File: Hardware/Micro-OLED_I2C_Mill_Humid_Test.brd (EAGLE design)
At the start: 20.3 x 29.2 mm, 5 parts

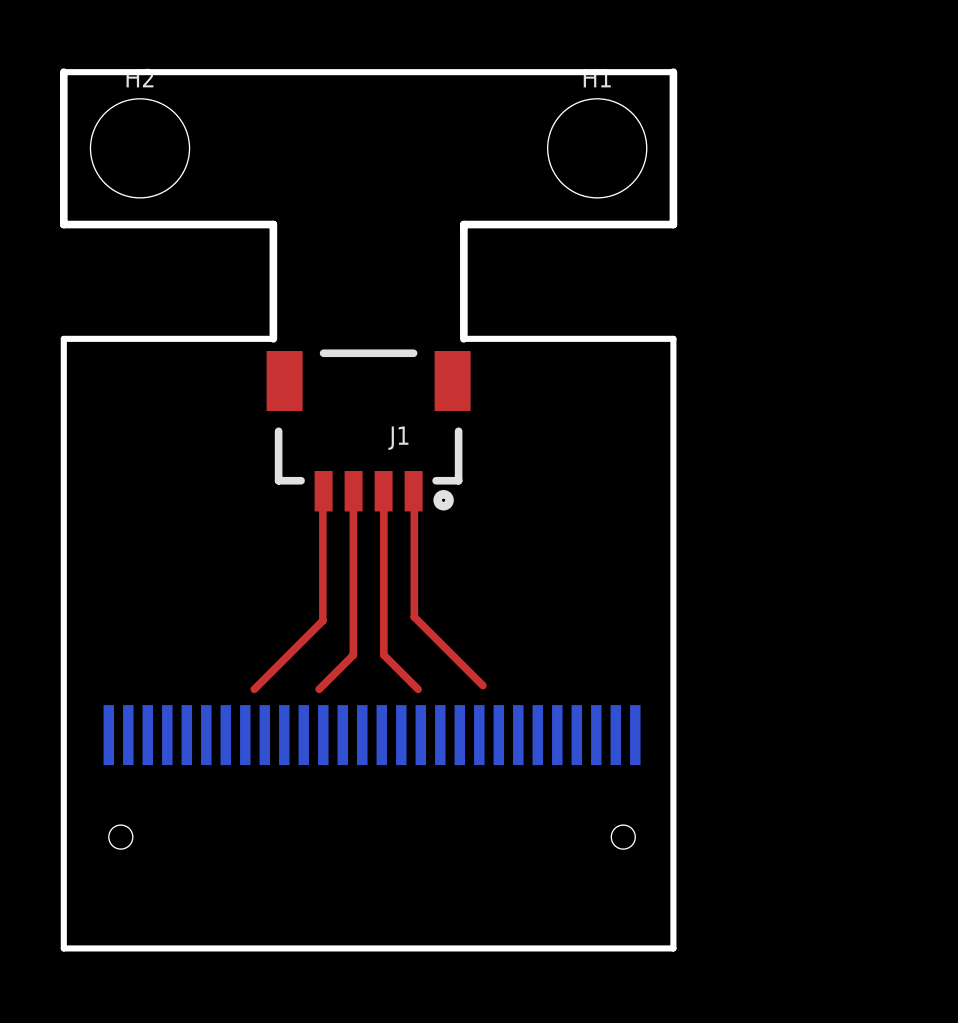
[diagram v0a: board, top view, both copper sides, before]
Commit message: More mold modifications Elongated the PCB for mold
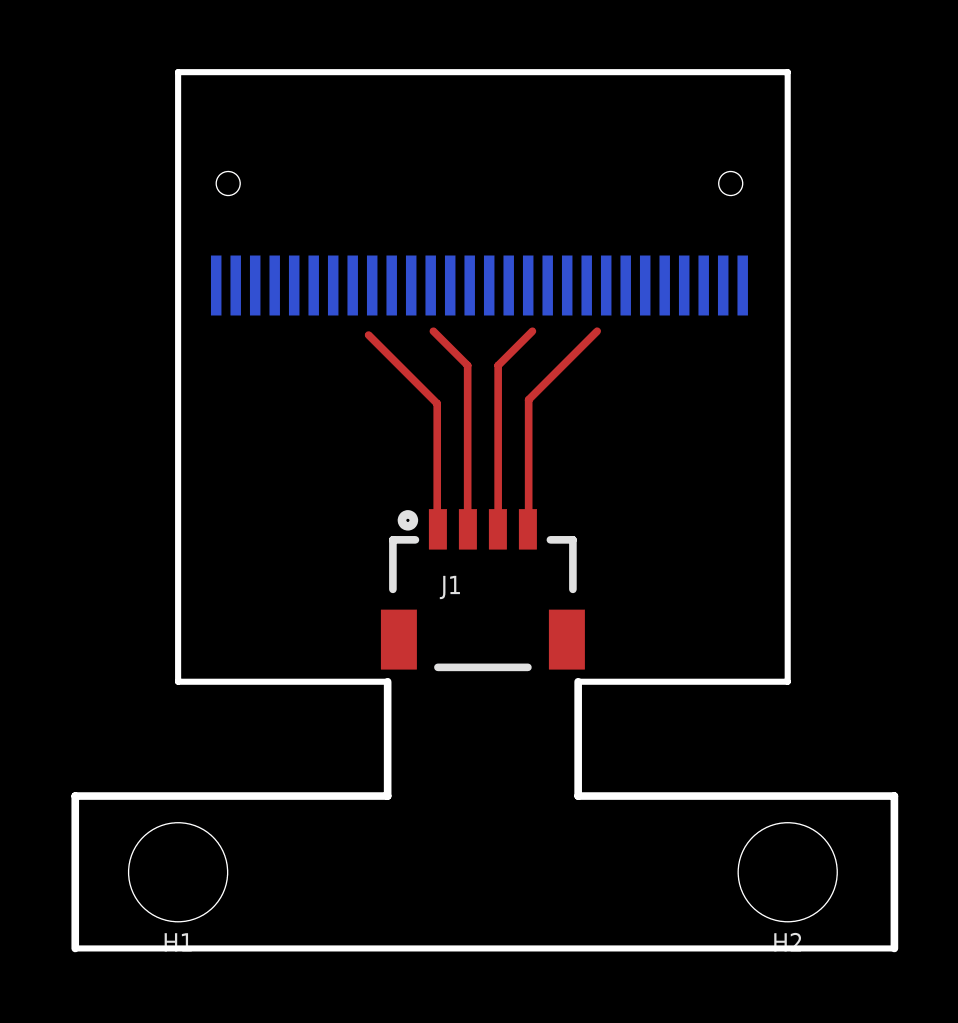
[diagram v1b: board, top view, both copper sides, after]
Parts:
- moved H2 32.4 mm to (24.1, 2.54), turned to 180 degrees
- moved H1 27.9 mm to (3.81, 2.54), turned to 180 degrees
- moved OLED1 20.5 mm to (5.08, 22.1), turned to 180 degrees
- moved J1 4.02 mm to (14.0, 14.0), turned to 0 degrees
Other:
- board size 20.3 x 29.2 mm -> 27.3 x 29.2 mm
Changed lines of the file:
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@@
 <layer number="47" name="Measures" color="7" fill="1" visible="no" active="yes"/>
 <layer number="48" name="Document" color="7" fill="1" visible="no" active="yes"/>
-<layer number="49" name="Reference" color="7" fill="1" visible="yes" active="yes"/>
+<layer number="49" name="Reference" color="7" fill="1" visible="no" active="yes"/>
 <layer number="50" name="dxf" color="7" fill="1" visible="no" active="no"/>
 <layer number="51" name="tDocu" color="6" fill="1" visible="yes" active="yes"/>
@@
 <board>
 <plain>
-<wire x1="20.32" y1="0" x2="20.32" y2="20.32" width="0.2032" layer="20"/>
-<wire x1="20.32" y1="20.32" x2="13.335" y2="20.32" width="0.2032" layer="20"/>
-<wire x1="6.985" y1="20.32" x2="0" y2="20.32" width="0.2032" layer="20"/>
-<wire x1="0" y1="20.32" x2="0" y2="0" width="0.2032" layer="20"/>
-<wire x1="0" y1="0" x2="20.32" y2="0" width="0.2032" layer="20"/>
+<wire x1="3.81" y1="29.21" x2="3.81" y2="8.89" width="0.2032" layer="20"/>
+<wire x1="3.81" y1="8.89" x2="10.795" y2="8.89" width="0.2032" layer="20"/>
+<wire x1="17.145" y1="8.89" x2="24.13" y2="8.89" width="0.2032" layer="20"/>
+<wire x1="24.13" y1="8.89" x2="24.13" y2="29.21" width="0.2032" layer="20"/>
+<wire x1="24.13" y1="29.21" x2="3.81" y2="29.21" width="0.2032" layer="20"/>
 <text x="-8.89" y="-19.05" size="1.778" layer="52" ratio="15" rot="MR0">Jim Lindblom</text>
 <wire x1="2.159" y1="-5.715" x2="2.921" y2="-5.715" width="0.254" layer="29"/>
-<wire x1="20.32" y1="29.21" x2="0" y2="29.21" width="0.2032" layer="20"/>
-<wire x1="0" y1="29.21" x2="0" y2="24.13" width="0.254" layer="20"/>
-<wire x1="0" y1="24.13" x2="6.985" y2="24.13" width="0.254" layer="20"/>
-<wire x1="13.335" y1="24.13" x2="20.32" y2="24.13" width="0.254" layer="20"/>
-<wire x1="20.32" y1="24.13" x2="20.32" y2="29.21" width="0.254" layer="20"/>
-<wire x1="6.985" y1="20.32" x2="6.985" y2="24.13" width="0.254" layer="20"/>
-<wire x1="13.335" y1="24.13" x2="13.335" y2="20.32" width="0.254" layer="20"/>
+<wire x1="0.381" y1="0" x2="27.686" y2="0" width="0.2032" layer="20"/>
+<wire x1="27.686" y1="0" x2="27.686" y2="5.08" width="0.254" layer="20"/>
+<wire x1="27.686" y1="5.08" x2="17.145" y2="5.08" width="0.254" layer="20"/>
+<wire x1="10.795" y1="5.08" x2="0.381" y2="5.08" width="0.254" layer="20"/>
+<wire x1="0.381" y1="5.08" x2="0.381" y2="0" width="0.254" layer="20"/>
+<wire x1="17.145" y1="8.89" x2="17.145" y2="5.08" width="0.254" layer="20"/>
+<wire x1="10.795" y1="5.08" x2="10.795" y2="8.89" width="0.254" layer="20"/>
 </plain>
 <attributes>
@@
 </autorouter>
 <elements>
-<element name="OLED1" library="microView-temp" package="OLED-0.66-64X48" value="OLED0.66" x="19.05" y="7.112" rot="MR0"/>
+<element name="OLED1" library="microView-temp" package="OLED-0.66-64X48" value="OLED0.66" x="5.08" y="22.098" rot="MR180"/>
 <element name="FRAME1" library="SparkFun-Aesthetics" package="CREATIVE_COMMONS" value="FRAME-LETTER" x="17.78" y="-19.05" rot="MR0"/>
-<element name="J1" library="SparkX" package="1X04_1MM_RA" value="" x="10.16" y="15.24" rot="R180"/>
-<element name="H1" library="SparkFun-Hardware" package="STAND-OFF" value="STAND-OFF" x="17.78" y="26.67"/>
-<element name="H2" library="SparkFun-Hardware" package="STAND-OFF" value="STAND-OFF" x="2.54" y="26.67"/>
+<element name="J1" library="SparkX" package="1X04_1MM_RA" value="" x="13.97" y="13.97"/>
+<element name="H1" library="SparkFun-Hardware" package="STAND-OFF" value="STAND-OFF" x="3.81" y="2.54" rot="R180"/>
+<element name="H2" library="SparkFun-Hardware" package="STAND-OFF" value="STAND-OFF" x="24.13" y="2.54" rot="R180"/>
 </elements>
 <signals>
@@
 </signal>
 <signal name="N$1">
-<wire x1="8.636" y1="15.24" x2="8.636" y2="10.922" width="0.254" layer="1"/>
-<wire x1="8.636" y1="10.922" x2="6.35" y2="8.636" width="0.254" layer="1"/>
+<wire x1="15.494" y1="13.97" x2="15.494" y2="18.288" width="0.254" layer="1"/>
+<wire x1="15.494" y1="18.288" x2="17.78" y2="20.574" width="0.254" layer="1"/>
 </signal>
 <signal name="N$2">
-<wire x1="9.652" y1="15.24" x2="9.652" y2="9.779" width="0.254" layer="1"/>
-<wire x1="9.652" y1="9.779" x2="8.509" y2="8.636" width="0.254" layer="1"/>
+<wire x1="14.478" y1="13.97" x2="14.478" y2="19.431" width="0.254" layer="1"/>
+<wire x1="14.478" y1="19.431" x2="15.621" y2="20.574" width="0.254" layer="1"/>
 </signal>
 <signal name="N$3">
-<wire x1="10.668" y1="15.24" x2="10.668" y2="9.779" width="0.254" layer="1"/>
-<wire x1="10.668" y1="9.779" x2="11.811" y2="8.636" width="0.254" layer="1"/>
+<wire x1="13.462" y1="13.97" x2="13.462" y2="19.431" width="0.254" layer="1"/>
+<wire x1="13.462" y1="19.431" x2="12.319" y2="20.574" width="0.254" layer="1"/>
 </signal>
 <signal name="N$4">
-<wire x1="11.684" y1="15.24" x2="11.684" y2="11.049" width="0.254" layer="1"/>
-<wire x1="11.684" y1="11.049" x2="13.97" y2="8.763" width="0.254" layer="1"/>
+<wire x1="12.446" y1="13.97" x2="12.446" y2="18.161" width="0.254" layer="1"/>
+<wire x1="12.446" y1="18.161" x2="10.16" y2="20.447" width="0.254" layer="1"/>
 </signal>
 </signals>

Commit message: Mold V2
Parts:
- J1: device SparkX:1X04_1MM_RA -> SparkX:1X04_1MM_RA_STRESSRELIEF
- moved H2 0.64 mm to (24.8, 2.54)
- moved H1 0.64 mm to (3.17, 2.54)
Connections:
- net D0/SCK: now also J1.2; no longer J1.4
- net VDD: now also J1.4; no longer J1.2
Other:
- outline, holes or cut-outs redrawn
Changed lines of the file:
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@@
 <plain>
 <wire x1="3.81" y1="29.21" x2="3.81" y2="8.89" width="0.2032" layer="20"/>
-<wire x1="3.81" y1="8.89" x2="10.795" y2="8.89" width="0.2032" layer="20"/>
-<wire x1="17.145" y1="8.89" x2="24.13" y2="8.89" width="0.2032" layer="20"/>
+<wire x1="3.81" y1="8.89" x2="5.715" y2="8.89" width="0.2032" layer="20"/>
+<wire x1="22.225" y1="8.89" x2="24.13" y2="8.89" width="0.2032" layer="20"/>
 <wire x1="24.13" y1="8.89" x2="24.13" y2="29.21" width="0.2032" layer="20"/>
 <wire x1="24.13" y1="29.21" x2="3.81" y2="29.21" width="0.2032" layer="20"/>
@@
 <wire x1="2.159" y1="-5.715" x2="2.921" y2="-5.715" width="0.254" layer="29"/>
 <wire x1="0.381" y1="0" x2="27.686" y2="0" width="0.2032" layer="20"/>
-<wire x1="27.686" y1="0" x2="27.686" y2="5.08" width="0.254" layer="20"/>
-<wire x1="27.686" y1="5.08" x2="17.145" y2="5.08" width="0.254" layer="20"/>
-<wire x1="10.795" y1="5.08" x2="0.381" y2="5.08" width="0.254" layer="20"/>
-<wire x1="0.381" y1="5.08" x2="0.381" y2="0" width="0.254" layer="20"/>
-<wire x1="17.145" y1="8.89" x2="17.145" y2="5.08" width="0.254" layer="20"/>
-<wire x1="10.795" y1="5.08" x2="10.795" y2="8.89" width="0.254" layer="20"/>
+<wire x1="27.686" y1="0" x2="27.686" y2="5.08" width="0.2032" layer="20"/>
+<wire x1="27.686" y1="5.08" x2="22.225" y2="5.08" width="0.2032" layer="20"/>
+<wire x1="5.715" y1="5.08" x2="0.381" y2="5.08" width="0.2032" layer="20"/>
+<wire x1="0.381" y1="5.08" x2="0.381" y2="0" width="0.2032" layer="20"/>
+<wire x1="22.225" y1="8.89" x2="22.225" y2="5.08" width="0.2032" layer="20"/>
+<wire x1="5.715" y1="5.08" x2="5.715" y2="8.89" width="0.2032" layer="20"/>
 </plain>
 <attributes>
@@
 <element name="OLED1" library="microView-temp" package="OLED-0.66-64X48" value="OLED0.66" x="5.08" y="22.098" rot="MR180"/>
 <element name="FRAME1" library="SparkFun-Aesthetics" package="CREATIVE_COMMONS" value="FRAME-LETTER" x="17.78" y="-19.05" rot="MR0"/>
-<element name="J1" library="SparkX" package="1X04_1MM_RA" value="" x="13.97" y="13.97"/>
-<element name="H1" library="SparkFun-Hardware" package="STAND-OFF" value="STAND-OFF" x="3.81" y="2.54" rot="R180"/>
-<element name="H2" library="SparkFun-Hardware" package="STAND-OFF" value="STAND-OFF" x="24.13" y="2.54" rot="R180"/>
+<element name="J1" library="SparkX" package="1X04_1MM_RA_STRESSRELIEF" value="" x="13.97" y="13.97"/>
+<element name="H1" library="SparkFun-Hardware" package="STAND-OFF" value="STAND-OFF" x="3.175" y="2.54" rot="R180"/>
+<element name="H2" library="SparkFun-Hardware" package="STAND-OFF" value="STAND-OFF" x="24.765" y="2.54" rot="R180"/>
 </elements>
 <signals>
@@
 </signal>
 <signal name="VDD">
-<contactref element="J1" pad="2"/>
+<contactref element="J1" pad="4"/>
 </signal>
 <signal name="D1/MOSI">
@@
 </signal>
 <signal name="D0/SCK">
-<contactref element="J1" pad="4"/>
+<contactref element="J1" pad="2"/>
 </signal>
 <signal name="N$1">
